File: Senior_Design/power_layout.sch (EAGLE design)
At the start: 104 parts, among them J1 AU-Y1008-2, J1[SIMCARD] 78646-3001, J2 U.FL-R-SMT-1(01), J3 U.FL-R-SMT-1(01), J4[GROVE] 640456-4, T1 BCX70SMD, T2 BCX70SMD, U1 SIM7000E, U2 TUSB2046BVFR, U3 MAX3373EEKA+T, U4 TPS2044BDR, X1 332-04

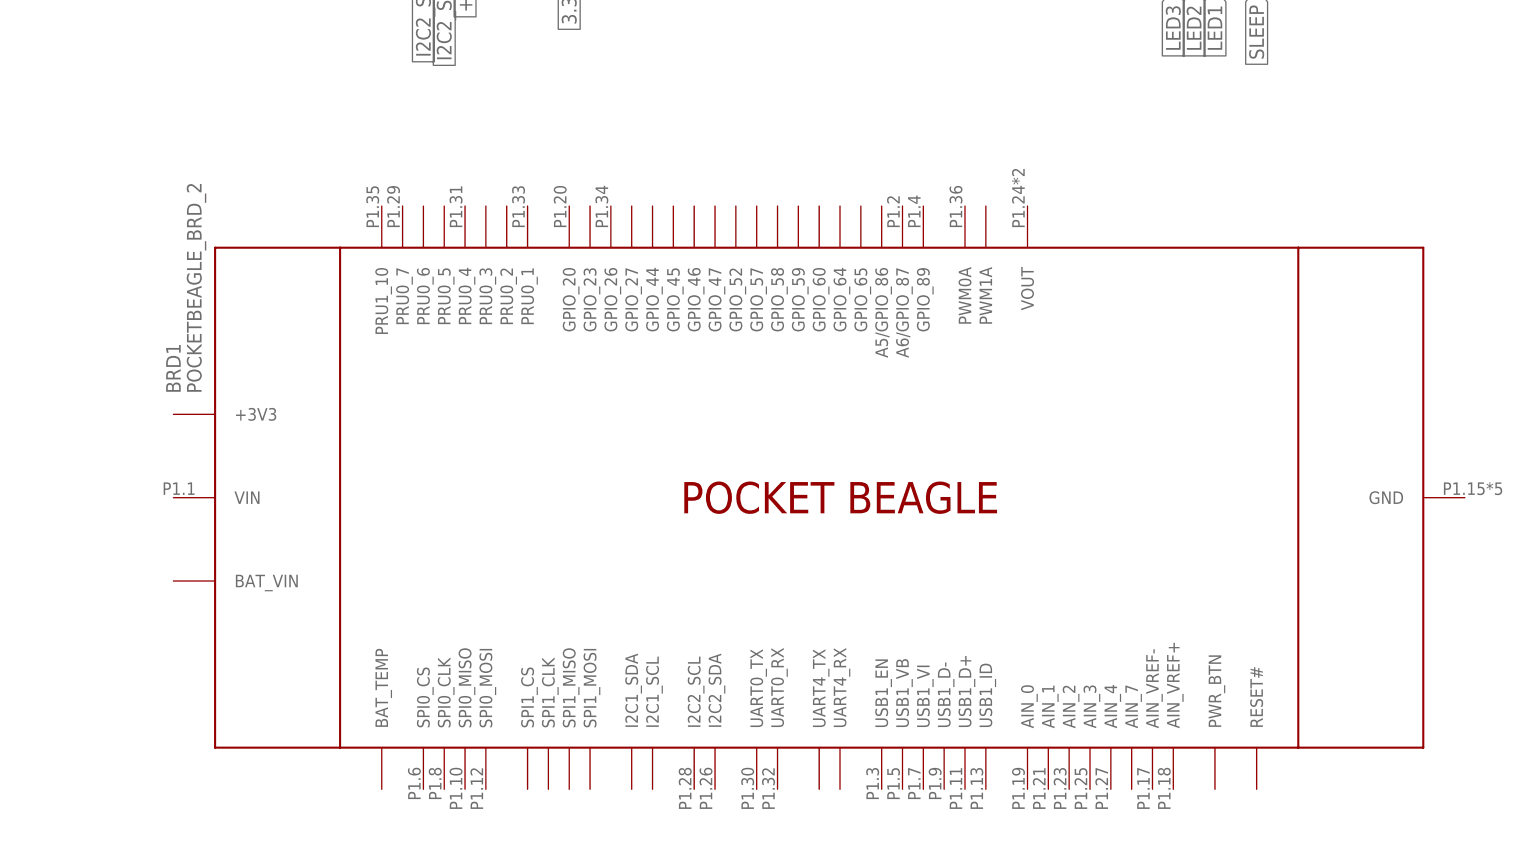
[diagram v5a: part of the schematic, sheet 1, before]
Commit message: Fixed issues w/ gerber files
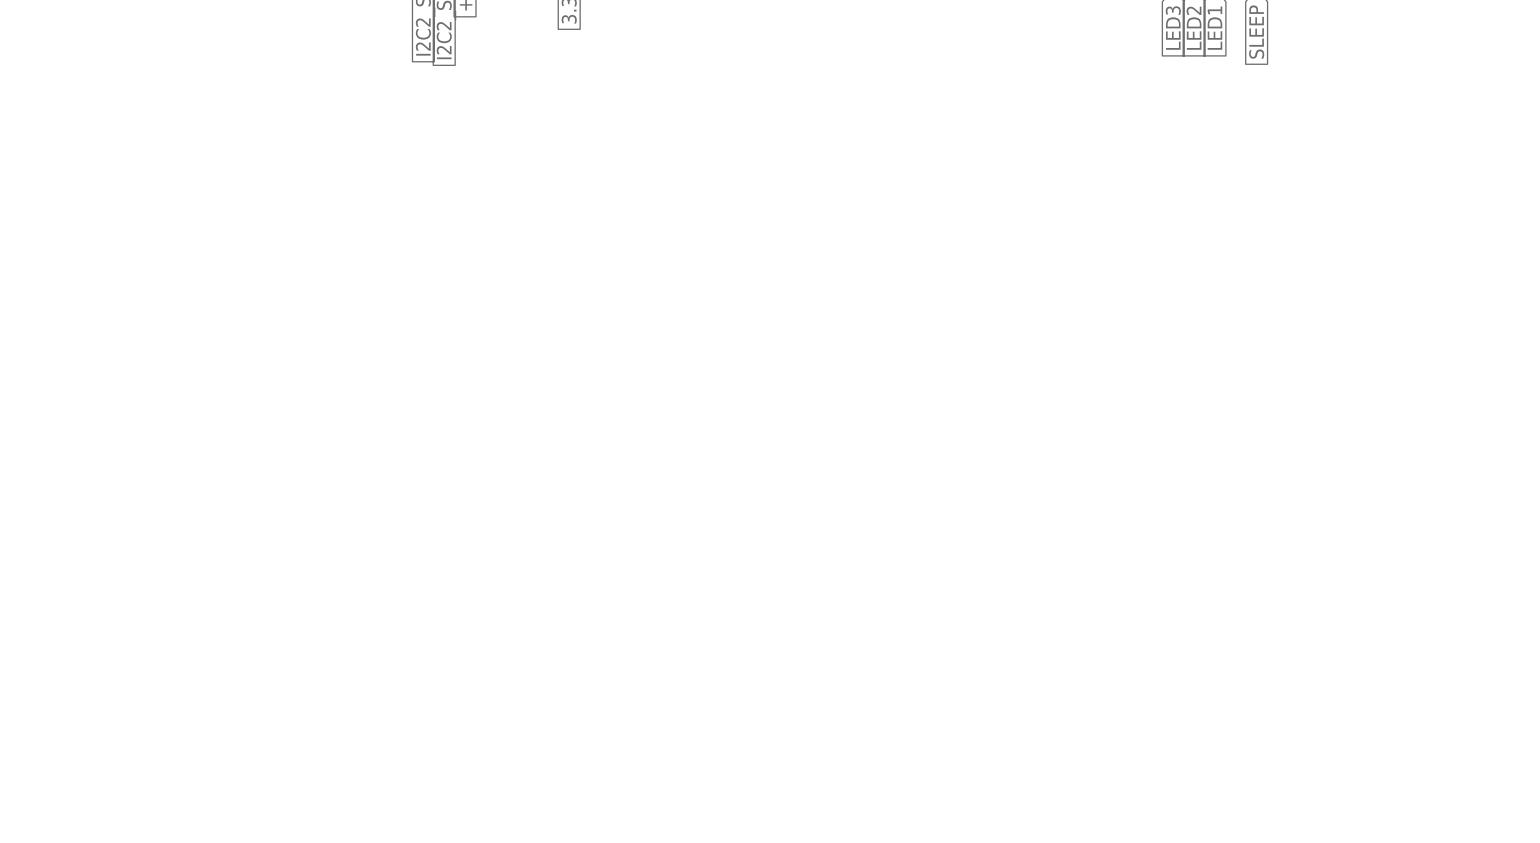
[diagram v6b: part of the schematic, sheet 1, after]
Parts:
- removed BRD1: POCKETBEAGLE_BRD_2, e14_BeagleBoard_PocketBeagle_v1_alpha1:POCKETBEAGLE_BRD_2
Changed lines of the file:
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@@
 <part name="C6" library="rcl" library_urn="urn:adsk.eagle:library:334" deviceset="C-US" device="C0805" package3d_urn="urn:adsk.eagle:package:23617/2"/>
 <part name="X_17" library="ngspice-simulation" library_urn="urn:adsk.eagle:library:527439" deviceset="GND" device=""/>
-<part name="BRD1" library="e14_BeagleBoard_PocketBeagle_v1_alpha1" deviceset="POCKETBEAGLE_?_2" device="BRD"/>
 <part name="J4[GROVE]" library="640456-4" deviceset="640456-4" device=""/>
 <part name="X_22" library="ngspice-simulation" library_urn="urn:adsk.eagle:library:527439" deviceset="GND" device=""/>
@@
 </instance>
 <instance part="X_17" gate="G$1" x="175.26" y="24.13" smashed="yes" rot="MR0" grouprefs="SIM7000"/>
-<instance part="BRD1" gate="G$1" x="99.06" y="-156.21" smashed="yes" rot="R90" grouprefs="POCKETBEAGLE_PINS">
-<attribute name="NAME" x="20.32" y="-143.51" size="1.778" layer="95" rot="R90" align="center-left"/>
-<attribute name="VALUE" x="22.86" y="-143.51" size="1.778" layer="96" rot="R90" align="center-left"/>
-</instance>
 <instance part="SV1" gate="G$1" x="63.5" y="-80.01" smashed="yes" rot="R90" grouprefs="POCKETBEAGLE_PINS">
 <attribute name="VALUE" x="88.9" y="-83.82" size="1.778" layer="96" rot="R90"/>

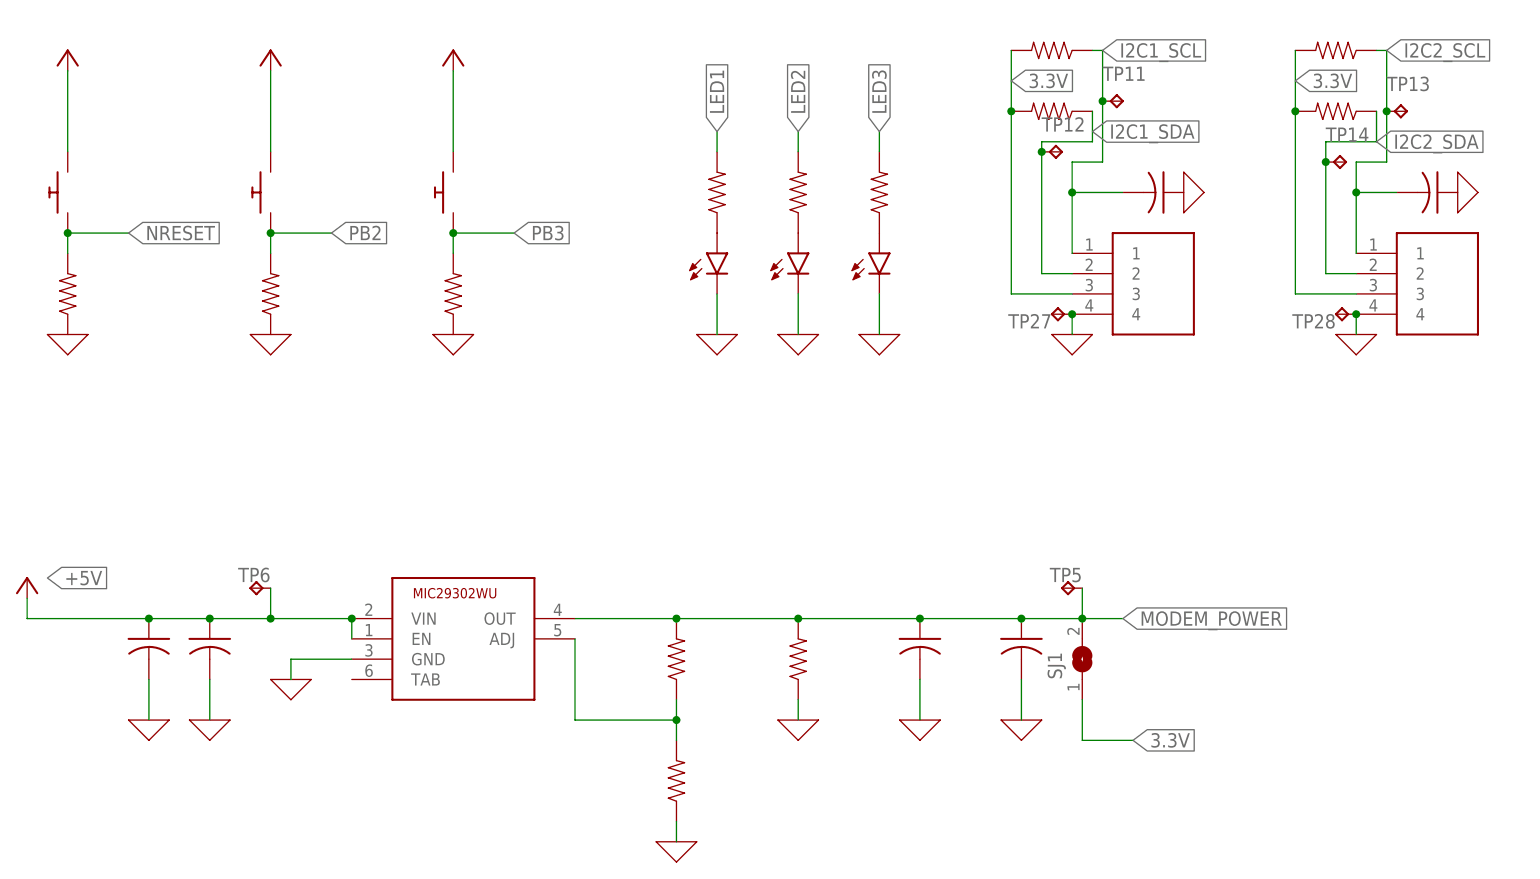
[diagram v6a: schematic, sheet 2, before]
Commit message: Alpha Order Design Changes
Incorporated all PCB Review design changes
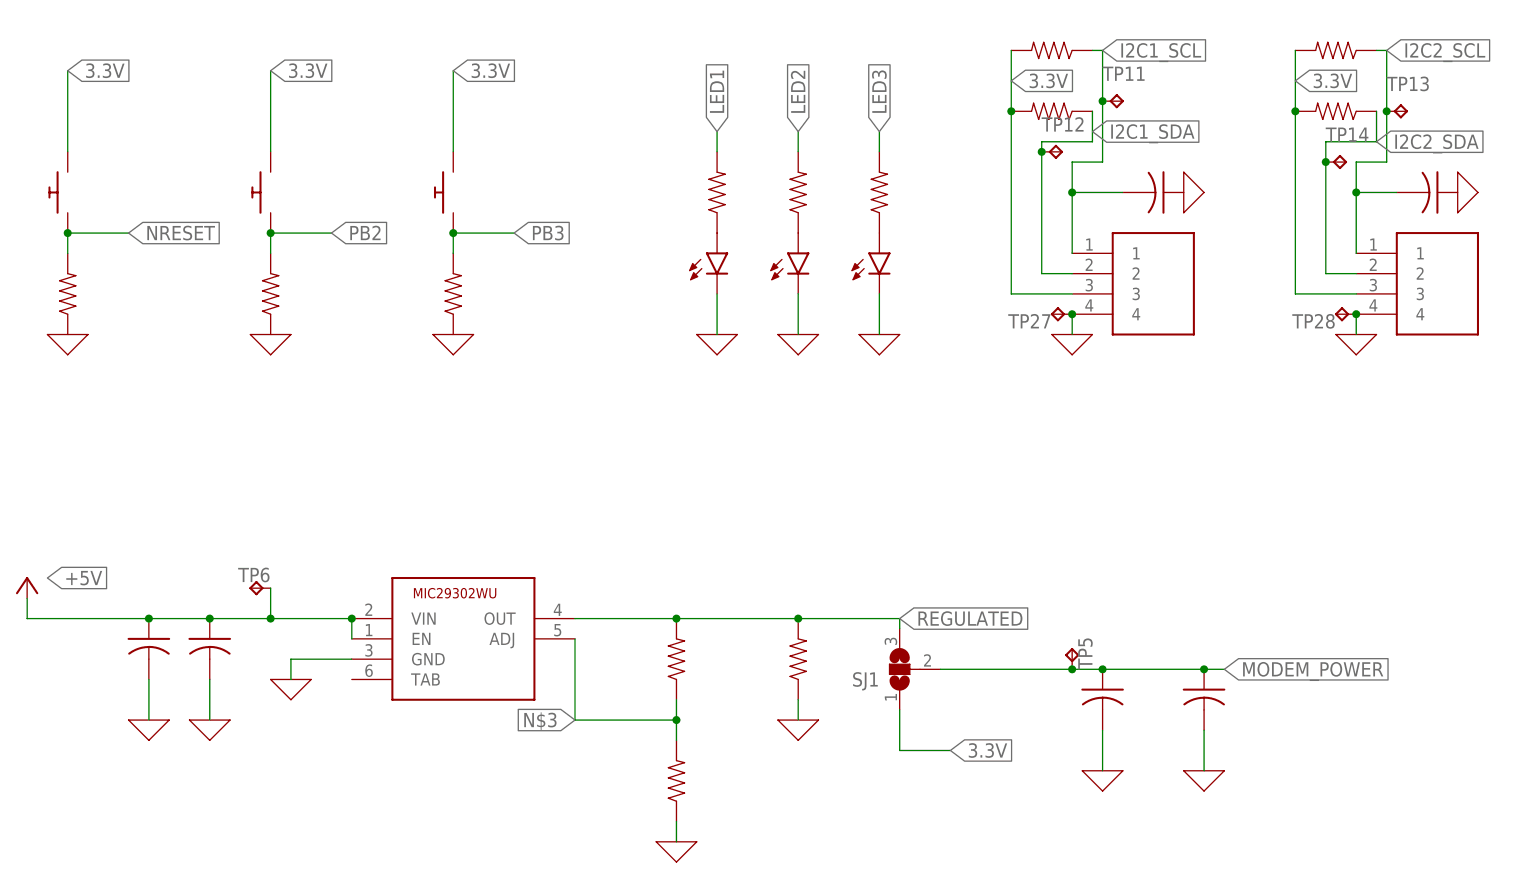
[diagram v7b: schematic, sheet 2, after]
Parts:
- removed TP20: TPTP10R, testpad:TPTP10R
- added D5: Yellow, SparkFun-LED:LED-YELLOW0603
- added R33: 330, SparkFun-Resistors:1KOHM-0603-1/10W-1%
- added SJ2: (no value), jumper:SJ
- SJ1: device jumper:SJ -> jumper:SJ2W
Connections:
- removed net N$15 (its old number): TP2.TP, U1.GNSS_ANT
- new net N$36: SJ2.2, U1.USB_VBUS
- new net N$37: D5.A, R33.1
- new net PRE_GPS: C16.2, TP2.TP, U1.GNSS_ANT
- new net REGULATED: POWER_SUPPLY.OUT, R5.2, R6.2, SJ1.3
- net +5V: now also SJ2.1; no longer SW1.P$2, SW2.P$2, SW3.P$2, U1.USB_VBUS
- net 3.3V: now also SW1.P$2, SW2.P$2, SW3.P$2
- net GND: now also D5.C; no longer C16.2
- net MODEM_POWER: no longer POWER_SUPPLY.OUT, R5.2, R6.2
- net N$33: now also R33.2; no longer TP20.TP
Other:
- moved on the sheet: C16, TP2, TP5

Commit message: Updated C3 Size and regenerated CAM
Part swap pre-ordering
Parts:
- C3: value (none) -> 330uF; device rcl:C-USC0805 -> rcl:C-USC1210
- C5: value (none) -> 100nF
- R1: value 330 -> 60.4
- R2, R3: value 330 -> 180
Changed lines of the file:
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@@
 <parts>
 <part name="C1" library="rcl" library_urn="urn:adsk.eagle:library:334" deviceset="C-US" device="C0805" package3d_urn="urn:adsk.eagle:package:23617/2"/>
-<part name="C3" library="rcl" library_urn="urn:adsk.eagle:library:334" deviceset="C-US" device="C0805" package3d_urn="urn:adsk.eagle:package:23617/2"/>
+<part name="C3" library="rcl" library_urn="urn:adsk.eagle:library:334" deviceset="C-US" device="C1210" package3d_urn="urn:adsk.eagle:package:23619/2" value="330uF"/>
 <part name="POWER_SUPPLY" library="MIC29302WU" deviceset="MIC29302WU" device=""/>
 <part name="X_1" library="ngspice-simulation" library_urn="urn:adsk.eagle:library:527439" deviceset="GND" device=""/>
@@
 <part name="X_5" library="ngspice-simulation" library_urn="urn:adsk.eagle:library:527439" deviceset="GND" device=""/>
 <part name="C4" library="rcl" library_urn="urn:adsk.eagle:library:334" deviceset="C-US" device="C0805" package3d_urn="urn:adsk.eagle:package:23617/2"/>
-<part name="C5" library="rcl" library_urn="urn:adsk.eagle:library:334" deviceset="C-US" device="C0805" package3d_urn="urn:adsk.eagle:package:23617/2"/>
+<part name="C5" library="rcl" library_urn="urn:adsk.eagle:library:334" deviceset="C-US" device="C0805" package3d_urn="urn:adsk.eagle:package:23617/2" value="100nF"/>
 <part name="X_6" library="ngspice-simulation" library_urn="urn:adsk.eagle:library:527439" deviceset="GND" device=""/>
 <part name="X_7" library="ngspice-simulation" library_urn="urn:adsk.eagle:library:527439" deviceset="GND" device=""/>
@@
 <part name="X_13" library="ngspice-simulation" library_urn="urn:adsk.eagle:library:527439" deviceset="GND" device=""/>
 <part name="GROVE1" library="640456-4" deviceset="640456-4" device=""/>
-<part name="R1" library="SparkFun-Resistors" library_urn="urn:adsk.eagle:library:532" deviceset="RESISTOR" device="0805" package3d_urn="urn:adsk.eagle:package:39651/1" value="330"/>
-<part name="R2" library="SparkFun-Resistors" library_urn="urn:adsk.eagle:library:532" deviceset="RESISTOR" device="0805" package3d_urn="urn:adsk.eagle:package:39651/1" value="330"/>
-<part name="R3" library="SparkFun-Resistors" library_urn="urn:adsk.eagle:library:532" deviceset="RESISTOR" device="0805" package3d_urn="urn:adsk.eagle:package:39651/1" value="330"/>
+<part name="R1" library="SparkFun-Resistors" library_urn="urn:adsk.eagle:library:532" deviceset="RESISTOR" device="0805" package3d_urn="urn:adsk.eagle:package:39651/1" value="60.4"/>
+<part name="R2" library="SparkFun-Resistors" library_urn="urn:adsk.eagle:library:532" deviceset="RESISTOR" device="0805" package3d_urn="urn:adsk.eagle:package:39651/1" value="180"/>
+<part name="R3" library="SparkFun-Resistors" library_urn="urn:adsk.eagle:library:532" deviceset="RESISTOR" device="0805" package3d_urn="urn:adsk.eagle:package:39651/1" value="180"/>
 <part name="R4" library="SparkFun-Resistors" library_urn="urn:adsk.eagle:library:532" deviceset="RESISTOR" device="0805" package3d_urn="urn:adsk.eagle:package:39651/1" value=" "/>
 <part name="R5" library="SparkFun-Resistors" library_urn="urn:adsk.eagle:library:532" deviceset="RESISTOR" device="0805" package3d_urn="urn:adsk.eagle:package:39651/1" value=" "/>
@@
 </instance>
 <instance part="U$1" gate="G$1" x="147.32" y="-31.75" smashed="yes" rot="MR0" grouprefs="SIM7000"/>
-<instance part="X1" gate="-1" x="-82.55" y="-15.24" smashed="yes" rot="R180" grouprefs="DBG_HDR SIM7000">
+<instance part="X1" gate="-1" x="-82.55" y="-15.24" smashed="yes" rot="R180" grouprefs="SIM7000 DBG_HDR">
 <attribute name="NAME" x="-85.09" y="-14.478" size="1.524" layer="95" rot="R180"/>
 <attribute name="VALUE" x="-81.788" y="-16.637" size="1.778" layer="96" rot="R180"/>
 </instance>
-<instance part="X1" gate="-2" x="-82.55" y="-12.7" smashed="yes" rot="R180" grouprefs="DBG_HDR SIM7000">
+<instance part="X1" gate="-2" x="-82.55" y="-12.7" smashed="yes" rot="R180" grouprefs="SIM7000 DBG_HDR">
 <attribute name="NAME" x="-85.09" y="-11.938" size="1.524" layer="95" rot="R180"/>
 </instance>
-<instance part="X1" gate="-3" x="-82.55" y="-10.16" smashed="yes" rot="R180" grouprefs="DBG_HDR SIM7000">
+<instance part="X1" gate="-3" x="-82.55" y="-10.16" smashed="yes" rot="R180" grouprefs="SIM7000 DBG_HDR">
 <attribute name="NAME" x="-85.09" y="-9.398" size="1.524" layer="95" rot="R180"/>
 </instance>
-<instance part="X1" gate="-4" x="-82.55" y="-7.62" smashed="yes" rot="R180" grouprefs="DBG_HDR SIM7000">
+<instance part="X1" gate="-4" x="-82.55" y="-7.62" smashed="yes" rot="R180" grouprefs="SIM7000 DBG_HDR">
 <attribute name="NAME" x="-85.09" y="-6.858" size="1.524" layer="95" rot="R180"/>
 </instance>
